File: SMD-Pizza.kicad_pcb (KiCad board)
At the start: 2 copper layers, 26.7 x 26.7 mm, 36 parts, among them Q1 AO3400, Q2 AO3400, Q3 AO3400, Q4 AO3400, Q5 AO3400, Q6 AO3400, Q7 AO3400

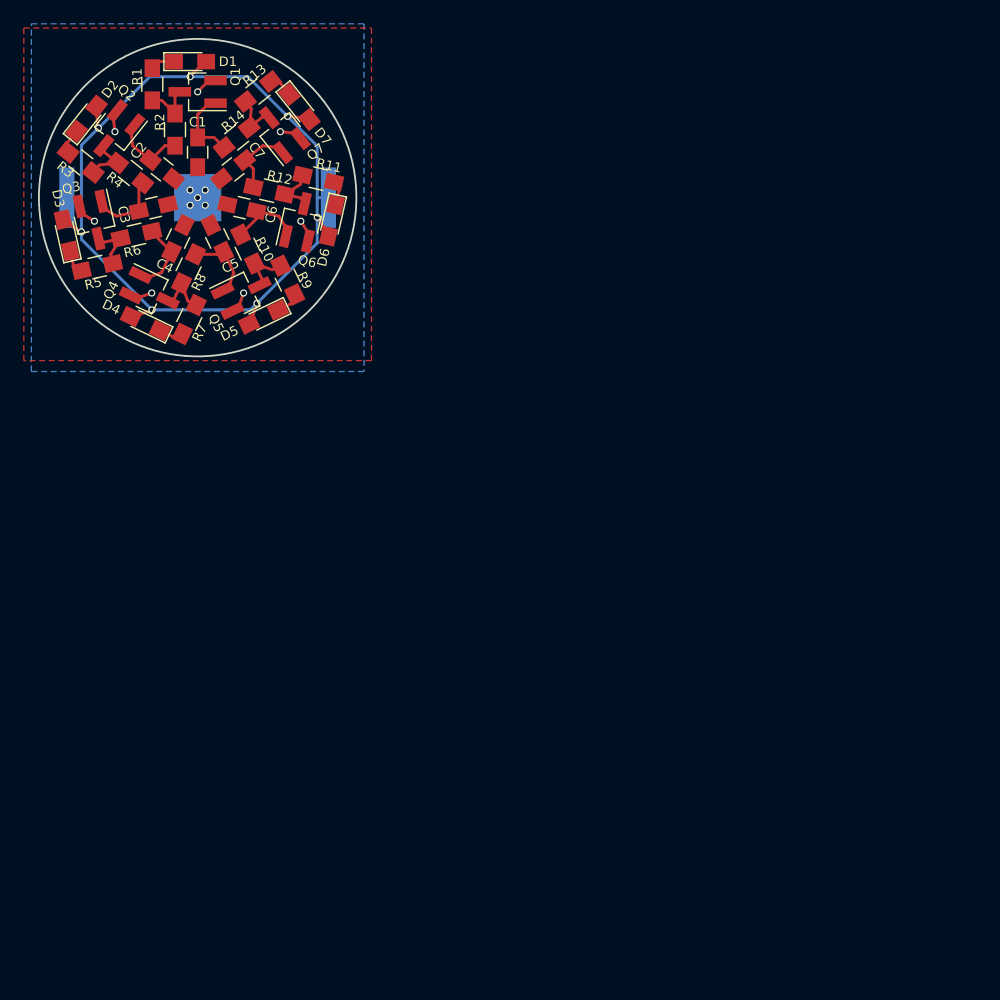
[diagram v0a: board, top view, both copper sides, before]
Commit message: added solder maks for better battery contact
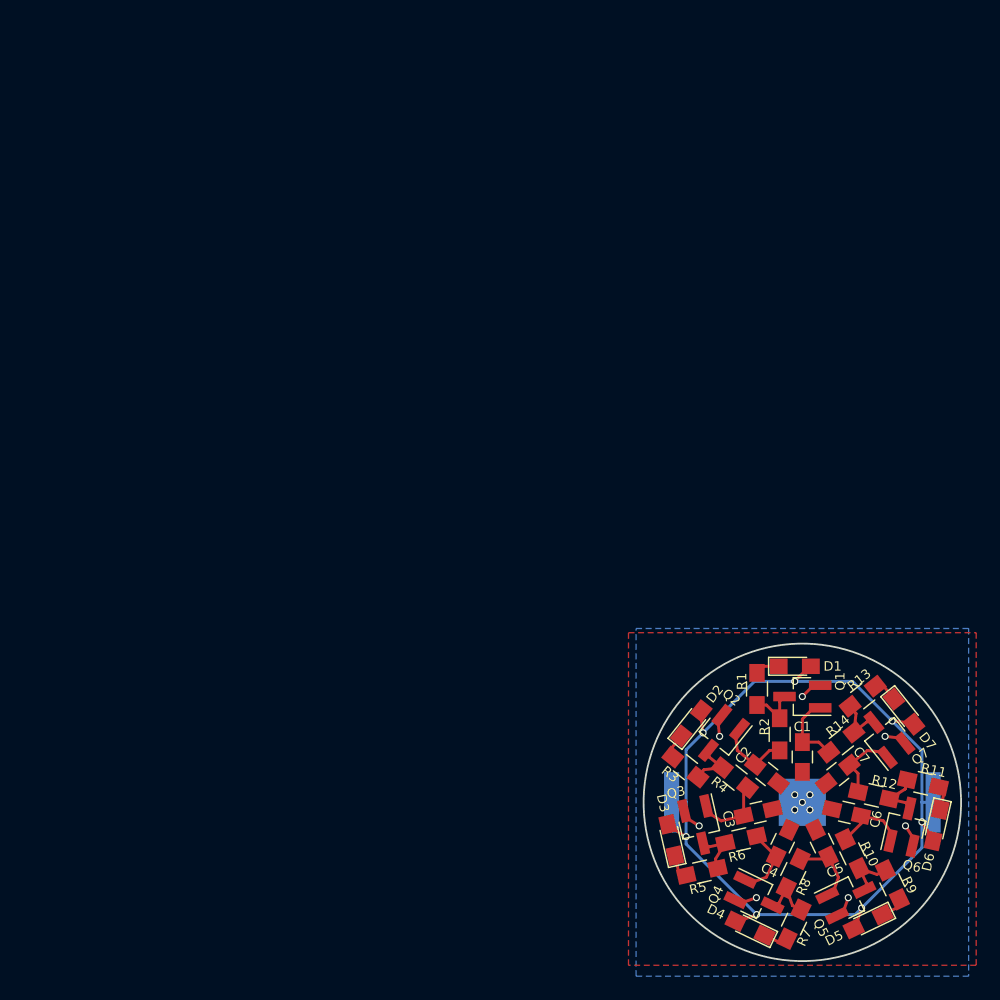
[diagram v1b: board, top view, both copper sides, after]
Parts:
- moved C4 71.8 mm to (49.1, 54.2)
- moved Q2 71.8 mm to (43.8, 45.3)
- moved R7 71.8 mm to (50.1, 61.0)
- moved BT1 71.8 mm to (50.8, 50.8)
- moved C1 71.8 mm to (50.8, 47.0)
- moved C2 71.8 mm to (47.8, 48.4)
- moved C3 71.8 mm to (47.1, 51.6)
- moved C5 71.8 mm to (52.5, 54.2)
- moved C6 71.8 mm to (54.5, 51.6)
- moved C7 71.8 mm to (53.8, 48.4)
- moved D1 71.8 mm to (50.2, 39.4)
- moved D2 71.8 mm to (41.5, 44.2)
- moved D3 71.8 mm to (39.8, 54.0)
- moved D4 71.8 mm to (46.4, 61.4)
- moved D5 71.8 mm to (56.3, 60.8)
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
